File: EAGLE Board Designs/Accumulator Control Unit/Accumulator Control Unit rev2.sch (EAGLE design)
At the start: 216 parts, among them J1 CONNECTOR-CAN_MF_T_V_, J2 CONNECTOR-8_MF_T_V_, J3 CONNECTOR-8_MF_T_V_, J4 CONNECTOR-2_MF_T_V_, J5 CONNECTOR-12_MF_T_V_, J6 CONNECTOR-14_MF_T_V_, Q1 TRANSISTOR_N_MOS__PMV15ENEA, Q2 TRANSISTOR_N_MOS__PMV15ENEA, Q3 TRANSISTOR_N_MOS__PMV15ENEA, Q4 TRANSISTOR_N_MOS__PMV15ENEA, T1 TRANSFORMER_HM2112ZNLT_AIRGAP, U1 RELAY_SOLIDSTATE_NO, U10 OPAMP_1_CHANNEL_OPA991, U11 LOGICGATE_AND_DCK3, U12 OPAMP_1_CHANNEL_OPA991, U13 OPAMP_1_CHANNEL_OPA991, U14 OPAMP_1_CHANNEL_OPA991, U15 LOGICGATE_AND_DCK3, U16 RELAY_SOLIDSTATE_NO, U17 VOLTAGE_REGULATOR_SOT223_3.3V, U18 OPAMP_1_CHANNEL_OPA991, U19 MAX7404, U2 ADG1423, U20 OPAMP_1_CHANNEL_OPA991, U22 OPAMP_1_CHANNEL_OPA991, U25 TCAN1051HQV-Q1, U26 MAX7404, U27 OPAMP_1_CHANNEL_OPA991, U28 MAX7404, U29 OPAMP_1_CHANNEL_OPA991, U3 LM555, U30 MAX7404, U4 OPAMP_1_CHANNEL_OPA991, U5 LTC6820, U6 ADM823, U7 OPAMP_1_CHANNEL_OPA991, U8 LOGICGATE_AND_DCK3, U9 OPAMP_1_CHANNEL_OPA991

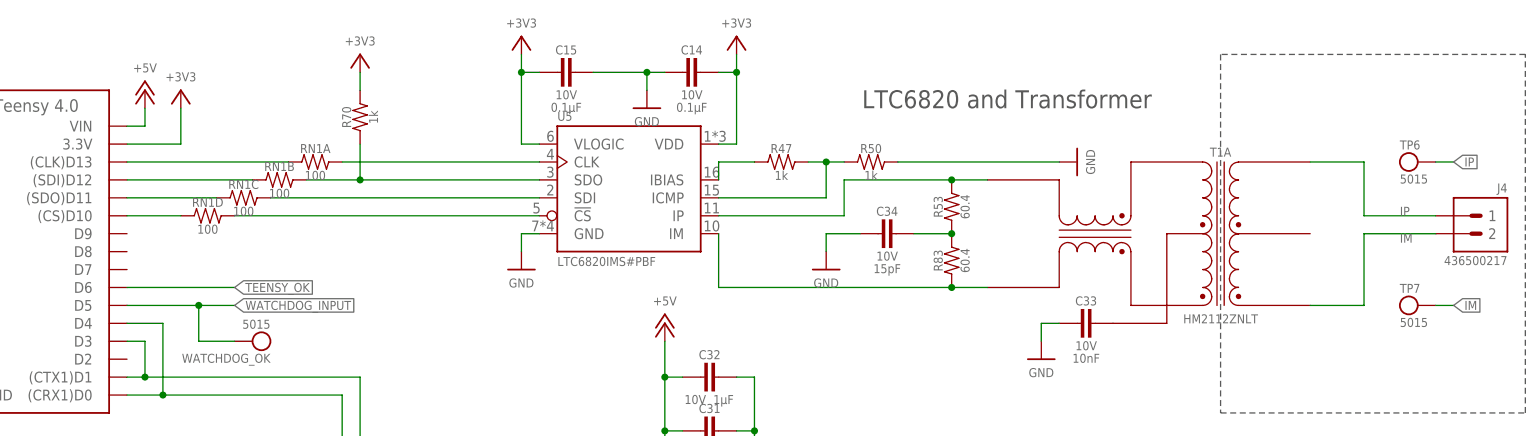
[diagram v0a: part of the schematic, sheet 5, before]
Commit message: updated isoSPI circuit and routed new board
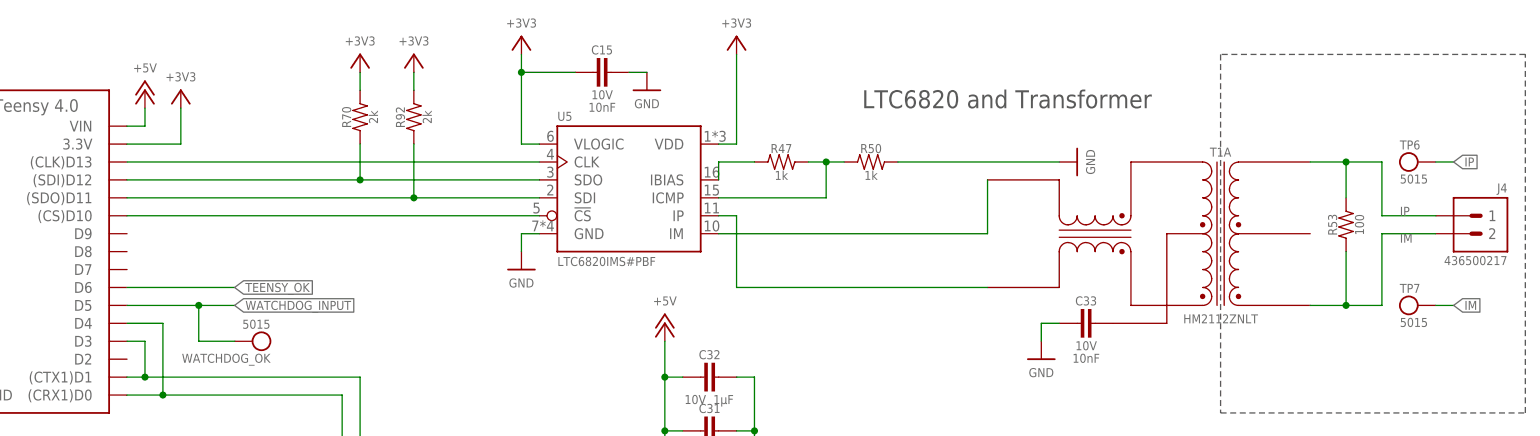
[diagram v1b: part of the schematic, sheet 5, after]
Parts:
- removed C14: CAPACITOR_0603_10V_0.1UF, HyTechDevices - Copy:CAPACITOR_0603_10V_0.1UF
- removed C34: CAPACITOR_0603_10V_15PF, HyTechDevices - Copy:CAPACITOR_0603_10V_15PF
- removed R83: RESISTOR_0603_60.4, HyTechDevices - Copy:RESISTOR_0603_60.4
- removed RN1: RESISTOR_NETWORK_4_100, HyTechDevices - Copy:RESISTOR_NETWORK_4_100
- added R92: RESISTOR_0603_2K, HyTechDevices:RESISTOR_0603_2K
- C15: value CAPACITOR_0603_10V_0.1UF -> CAPACITOR_0603_10V_10NF; device HyTechDevices - Copy:CAPACITOR_0603_10V_0.1UF -> HyTechDevices:CAPACITOR_0603_10V_10NF
- R53: value RESISTOR_0603_60.4 -> RESISTOR_0603_100; device HyTechDevices - Copy:RESISTOR_0603_60.4 -> HyTechDevices:RESISTOR_0603_100
- R70: value RESISTOR_0603_1K -> RESISTOR_0603_2K; device HyTechDevices - Copy:RESISTOR_0603_1K -> HyTechDevices:RESISTOR_0603_2K
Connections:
- net TSAL_GREEN1 renamed N$18
- net TSAL_RED1 renamed N$19
- removed net N$18 (its old number): RN1C.2, U5.SDI
- removed net N$19 (its old number): A1.(CS)D10, RN1D.1
- removed net N$21: A1.(SDO)D11, RN1C.1
- removed net N$38: R83.1, T1A.TD+, U5.IM
- removed net N$42: C34.1, R53.1, R83.2
- net +3V3: now also R92.2; no longer C14.1
- net CS_LTC_6820: now also A1.(CS)D10; no longer RN1D.2
- net GND: no longer C14.2, C34.2
- net IM: now also R53.1
- net IP: now also R53.2
- net N$13: now also A1.(SDO)D11, R92.1, U5.SDI; no longer RN1A.2, U5.CLK
- net N$15: now also T1A.TD-, U5.IM; no longer R70.1, RN1B.2, U5.SDO
- net N$35: now also T1A.TD+; no longer R53.2, T1A.TD-
- net N$43: now also R70.1, U5.SDO; no longer RN1B.1
- net N$44: now also U5.CLK; no longer RN1A.1
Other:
- moved on the sheet: C15, R53

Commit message: changes
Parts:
- removed F1: FUSE_MINI-BLADE_1A, HyTechDevices - Copy:FUSE_MINI-BLADE_1A
- added C14: CAPACITOR_0603_10V_0.1UF, HyTechDevices:CAPACITOR_0603_10V_0.1UF
- added U21: LOGICGATE_BUFFER, HyTechDevices:LOGICGATE_BUFFER
- added XF1: FUSE_HOLDER_MINIBLADEPTH, HyTechDevices:FUSE_HOLDER_MINIBLADEPTH
- T1: device HyTechDevices - Copy:TRANSFORMER_HM2112ZNLT_AIRGAP -> HyTechDevices:TRANSFORMER_HM2112ZNLT_AIRGAP
- TP_12V: SIGNAL (none) -> +12V
- TP_3.3V: SIGNAL (none) -> +3V3
- TP_5V: SIGNAL (none) -> +5V
- TP_GND: SIGNAL (none) -> GND
- TP_TSAL_GREEN: SIGNAL (none) -> N$18
- TP_TSAL_RED: SIGNAL (none) -> N$19
- U6: value ADM823 -> ADM8316WBX30; device HyTechDevices - Copy:ADM823 -> HyTechDevices:ADM8316WBX30
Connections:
- removed net N$35: T1A.TD+, U5.IP
- new net TD+: J4.1, R53.2, T1A.MX+, TP6.P$1
- new net TD-: J4.2, R53.1, T1A.MX-, TP7.P$1
- net +12V: now also XF1.2; no longer F1.2
- net +3V3: now also C14.1, U21P.VDD
- net 12VIN: now also XF1.1; no longer F1.1
- net AMS_OK_3.3V: now also U21A.OUT; no longer R13.2, U6.!RESET!
- net GND: now also C14.2, U21P.GND
- net IM: now also T1A.TD-, U5.IM; no longer J4.2, R53.1, T1A.MX+, TP7.P$1
- net IP: now also T1A.TD+, U5.IP; no longer J4.1, R53.2, T1A.MX-, TP6.P$1
- net N$15: now also R13.2, U21A.IN, U6.!RESET!; no longer T1A.TD-, U5.IM

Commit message: more changes to rev2
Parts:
- removed D12, D5, D7, D8, D9: SCHOTTKY, HyTechDevices:SCHOTTKY
- R59: value RESISTOR_0603_1K -> RESISTOR_0603_10K; device HyTechDevices - Copy:RESISTOR_0603_1K -> HyTechDevices:RESISTOR_0603_10K
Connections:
- removed net N$31: D7.C, R23.1
- removed net N$32: D5.C, R14.1
- removed net N$33: D8.C, R39.1
- removed net N$34: D9.C, R44.1
- removed net N$40: D12.C, R51.1
- net +12V: now also R39.1; no longer D8.A
- net BSPD_CURRENT: now also R44.1; no longer D9.A
- net IMD_OK: now also R14.1; no longer D5.A
- net MHS: now also R51.1; no longer D12.A
- net PRECHARGE_OK: now also R23.1; no longer D7.A
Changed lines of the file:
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@@
 <part name="P58" library="HyTechSupplies" deviceset="GND" device=""/>
 <part name="P59" library="HyTechSupplies" deviceset="GND" device=""/>
-<part name="D5" library="HyTechDevices" deviceset="SCHOTTKY" device=""/>
 <part name="R14" library="HyTechDevices - Copy" deviceset="RESISTOR_?_*" device="0603" technology="43K"/>
 <part name="R15" library="HyTechDevices - Copy" deviceset="RESISTOR_?_*" device="0603" technology="12K"/>
 <part name="P66" library="HyTechSupplies" deviceset="GND" device=""/>
-<part name="D7" library="HyTechDevices" deviceset="SCHOTTKY" device=""/>
 <part name="P67" library="HyTechSupplies" deviceset="GND" device=""/>
-<part name="D8" library="HyTechDevices" deviceset="SCHOTTKY" device=""/>
 <part name="R39" library="HyTechDevices - Copy" deviceset="RESISTOR_?_*" device="0603" technology="43K"/>
 <part name="P68" library="HyTechSupplies" deviceset="GND" device=""/>
-<part name="D9" library="HyTechDevices" deviceset="SCHOTTKY" device=""/>
 <part name="R44" library="HyTechDevices - Copy" deviceset="RESISTOR_?_*" device="0603" technology="43K"/>
 <part name="P69" library="HyTechSupplies" deviceset="GND" device=""/>
@@
 <part name="R13" library="HyTechDevices - Copy" deviceset="RESISTOR_?_*" device="0603" technology="100K"/>
 <part name="C36" library="HyTechDevices - Copy" deviceset="CAPACITOR_?_*" device="0603" technology="10V_0.1UF"/>
-<part name="R59" library="HyTechDevices - Copy" deviceset="RESISTOR_?_*" device="0603" technology="1K"/>
+<part name="R59" library="HyTechDevices" deviceset="RESISTOR_?_*" device="0603" technology="10K" value="RESISTOR_0603_10K"/>
 <part name="P31" library="HyTechSupplies" deviceset="GND" device=""/>
 <part name="R60" library="HyTechDevices - Copy" deviceset="RESISTOR_?_*" device="0603" technology="10K"/>
@@
 <part name="P82" library="HyTechSupplies" deviceset="GND" device=""/>
 <part name="C43" library="HyTechDevices - Copy" deviceset="CAPACITOR_?_*" device="0603" technology="10V_680PF"/>
-<part name="D12" library="HyTechDevices" deviceset="SCHOTTKY" device=""/>
 <part name="R52" library="HyTechDevices - Copy" deviceset="RESISTOR_?_*" device="0603" technology="12K"/>
 <part name="P87" library="HyTechSupplies" deviceset="GND" device=""/>
@@
 <plain>
 <text x="129.54" y="20.32" size="2.54" layer="95">Josh Kirshenbaum</text>
-<text x="22.86" y="71.12" size="1.778" layer="97">12V to 3.3V</text>
-<text x="20.32" y="106.68" size="1.778" layer="97">12V to 3.3V</text>
-<text x="22.86" y="53.34" size="1.778" layer="97">5V to 3.3V</text>
-<text x="33.02" y="91.44" size="1.778" layer="97">12V to 3.3V</text>
+<text x="30.48" y="71.12" size="1.778" layer="97">12V to 3.3V</text>
+<text x="27.94" y="106.68" size="1.778" layer="97">12V to 3.3V</text>
+<text x="30.48" y="53.34" size="1.778" layer="97">5V to 3.3V</text>
+<text x="40.64" y="91.44" size="1.778" layer="97">12V to 3.3V</text>
 <text x="203.2" y="101.6" size="2.54" layer="97">Watchdog Timer</text>
 <text x="40.64" y="114.3" size="2.54" layer="97">Voltage Dividers</text>
@@
 <wire x1="271.78" y1="137.16" x2="271.78" y2="187.96" width="0.1524" layer="97" style="shortdash"/>
 <wire x1="271.78" y1="187.96" x2="228.6" y2="187.96" width="0.1524" layer="97" style="shortdash"/>
-<text x="20.32" y="38.1" size="1.778" layer="97">10V to 3.3V</text>
+<text x="27.94" y="38.1" size="1.778" layer="97">10V to 3.3V</text>
 </plain>
 <instances>
@@
 <attribute name="VALUE" x="45.72" y="133.35" size="1.27" layer="96" align="top-center"/>
 </instance>
-<instance part="D5" gate="G$1" x="40.64" y="104.14" smashed="yes">
-<attribute name="NAME" x="39.37" y="106.045" size="1.27" layer="95" align="bottom-center"/>
-<attribute name="MPN" x="39.37" y="102.235" size="1.27" layer="96" align="top-center"/>
-</instance>
 <instance part="R14" gate="G$1" x="53.34" y="104.14" smashed="yes">
 <attribute name="NAME" x="52.07" y="105.41" size="1.27" layer="95" align="bottom-center"/>
@@
 <attribute name="VALUE" x="78.74" y="97.79" size="1.27" layer="96" align="top-center"/>
 </instance>
-<instance part="D7" gate="G$1" x="40.64" y="50.8" smashed="yes">
-<attribute name="NAME" x="39.37" y="52.705" size="1.27" layer="95" align="bottom-center"/>
-<attribute name="MPN" x="39.37" y="48.895" size="1.27" layer="96" align="top-center"/>
-</instance>
 <instance part="P67" gate="1" x="78.74" y="45.72" smashed="yes">
 <attribute name="VALUE" x="78.74" y="44.45" size="1.27" layer="96" align="top-center"/>
 </instance>
-<instance part="D8" gate="G$1" x="40.64" y="86.36" smashed="yes">
-<attribute name="NAME" x="39.37" y="88.265" size="1.27" layer="95" align="bottom-center"/>
-<attribute name="MPN" x="39.37" y="84.455" size="1.27" layer="96" align="top-center"/>
-</instance>
 <instance part="R39" gate="G$1" x="53.34" y="86.36" smashed="yes">
 <attribute name="NAME" x="52.07" y="87.63" size="1.27" layer="95" align="bottom-center"/>
@@
 <attribute name="VALUE" x="78.74" y="80.01" size="1.27" layer="96" align="top-center"/>
 </instance>
-<instance part="D9" gate="G$1" x="40.64" y="68.58" smashed="yes">
-<attribute name="NAME" x="39.37" y="70.485" size="1.27" layer="95" align="bottom-center"/>
-<attribute name="MPN" x="39.37" y="66.675" size="1.27" layer="96" align="top-center"/>
-</instance>
 <instance part="R44" gate="G$1" x="53.34" y="68.58" smashed="yes">
 <attribute name="NAME" x="52.07" y="69.85" size="1.27" layer="95" align="bottom-center"/>
@@
 <attribute name="VALUE" x="78.74" y="62.23" size="1.27" layer="96" align="top-center"/>
 </instance>
-<instance part="P70" gate="1" x="30.48" y="91.44" smashed="yes">
-<attribute name="VALUE" x="30.48" y="95.25" size="1.27" layer="96" align="bottom-center"/>
+<instance part="P70" gate="1" x="38.1" y="91.44" smashed="yes">
+<attribute name="VALUE" x="38.1" y="95.25" size="1.27" layer="96" align="bottom-center"/>
 </instance>
 <instance part="R30" gate="G$1" x="71.12" y="50.8" smashed="yes">
@@
 <attribute name="RESISTANCE" x="201.93" y="87.63" size="1.27" layer="96" rot="R90" align="top-center"/>
 </instance>
-<instance part="D12" gate="G$1" x="40.64" y="35.56" smashed="yes">
-<attribute name="NAME" x="39.37" y="37.465" size="1.27" layer="95" align="bottom-center"/>
-<attribute name="MPN" x="39.37" y="33.655" size="1.27" layer="96" align="top-center"/>
-</instance>
 <instance part="R52" gate="G$1" x="71.12" y="35.56" smashed="yes">
 <attribute name="NAME" x="69.85" y="36.83" size="1.27" layer="95" align="bottom-center"/>
@@
 <net name="BSPD_CURRENT" class="0">
 <segment>
-<pinref part="D9" gate="G$1" pin="A"/>
-<wire x1="35.56" y1="68.58" x2="33.02" y2="68.58" width="0.1524" layer="91"/>
-<label x="33.02" y="68.58" size="1.27" layer="95" rot="R180" xref="yes"/>
+<label x="40.64" y="68.58" size="1.27" layer="95" rot="R180" xref="yes"/>
+<pinref part="R44" gate="G$1" pin="1"/>
+<wire x1="40.64" y1="68.58" x2="48.26" y2="68.58" width="0.1524" layer="91"/>
 </segment>
 </net>
 <net name="IMD_OK" class="0">
 <segment>
-<pinref part="D5" gate="G$1" pin="A"/>
-<wire x1="35.56" y1="104.14" x2="33.02" y2="104.14" width="0.1524" layer="91"/>
-<label x="33.02" y="104.14" size="1.27" layer="95" rot="R180" xref="yes"/>
-</segment>
-</net>
-<net name="N$32" class="0">
-<segment>
-<pinref part="D5" gate="G$1" pin="C"/>
+<label x="40.64" y="104.14" size="1.27" layer="95" rot="R180" xref="yes"/>
 <pinref part="R14" gate="G$1" pin="1"/>
-<wire x1="43.18" y1="104.14" x2="48.26" y2="104.14" width="0.1524" layer="91"/>
-</segment>
-</net>
-<net name="N$31" class="0">
-<segment>
-<pinref part="D7" gate="G$1" pin="C"/>
-<wire x1="43.18" y1="50.8" x2="48.26" y2="50.8" width="0.1524" layer="91"/>
-<pinref part="R23" gate="G$1" pin="1"/>
-</segment>
-</net>
-<net name="N$33" class="0">
-<segment>
-<pinref part="D8" gate="G$1" pin="C"/>
-<pinref part="R39" gate="G$1" pin="1"/>
-<wire x1="43.18" y1="86.36" x2="48.26" y2="86.36" width="0.1524" layer="91"/>
-</segment>
-</net>
-<net name="N$34" class="0">
-<segment>
-<pinref part="D9" gate="G$1" pin="C"/>
-<pinref part="R44" gate="G$1" pin="1"/>
-<wire x1="43.18" y1="68.58" x2="48.26" y2="68.58" width="0.1524" layer="91"/>
+<wire x1="40.64" y1="104.14" x2="48.26" y2="104.14" width="0.1524" layer="91"/>
 </segment>
 </net>
@@
 <net name="PRECHARGE_OK" class="0">
 <segment>
-<pinref part="D7" gate="G$1" pin="A"/>
-<wire x1="35.56" y1="50.8" x2="33.02" y2="50.8" width="0.1524" layer="91"/>
-<label x="33.02" y="50.8" size="1.27" layer="95" rot="R180" xref="yes"/>
+<label x="40.64" y="50.8" size="1.27" layer="95" rot="R180" xref="yes"/>
+<pinref part="R23" gate="G$1" pin="1"/>
+<wire x1="40.64" y1="50.8" x2="48.26" y2="50.8" width="0.1524" layer="91"/>
 </segment>
 </net>
 <net name="+12V" class="0">
 <segment>
-<pinref part="D8" gate="G$1" pin="A"/>
-<wire x1="35.56" y1="86.36" x2="30.48" y2="86.36" width="0.1524" layer="91"/>
-<wire x1="30.48" y1="86.36" x2="30.48" y2="88.9" width="0.1524" layer="91"/>
+<wire x1="38.1" y1="86.36" x2="38.1" y2="88.9" width="0.1524" layer="91"/>
 <pinref part="P70" gate="1" pin="+12V"/>
+<pinref part="R39" gate="G$1" pin="1"/>
+<wire x1="38.1" y1="86.36" x2="48.26" y2="86.36" width="0.1524" layer="91"/>
 </segment>
 </net>
@@
 </segment>
 </net>
-<net name="N$40" class="0">
-<segment>
-<pinref part="D12" gate="G$1" pin="C"/>
-<wire x1="43.18" y1="35.56" x2="48.26" y2="35.56" width="0.1524" layer="91"/>
-<pinref part="R51" gate="G$1" pin="1"/>
-</segment>
-</net>
 <net name="MHS" class="0">
 <segment>
-<pinref part="D12" gate="G$1" pin="A"/>
-<wire x1="35.56" y1="35.56" x2="33.02" y2="35.56" width="0.1524" layer="91"/>
-<label x="33.02" y="35.56" size="1.27" layer="95" rot="R180" xref="yes"/>
+<label x="40.64" y="35.56" size="1.27" layer="95" rot="R180" xref="yes"/>
+<pinref part="R51" gate="G$1" pin="1"/>
+<wire x1="40.64" y1="35.56" x2="48.26" y2="35.56" width="0.1524" layer="91"/>
 </segment>
 </net>
